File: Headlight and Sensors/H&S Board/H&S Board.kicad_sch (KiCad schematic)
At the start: 37 parts, among them J1 XT60-M, J2 XT60-M, J3 22035035, J4 Molex Micro-Fit 4 Pin, J5 XT60-M, J6 XT60-M, J7 DAQ Board, J8 Driver UI, J9 XT60-M, Q1 PSMN1R8-40YLC,115, Q2 PSMN1R8-40YLC,115, Q3 PSMN1R8-40YLC,115, U1 ASM330LHHTR, U2 UA78M05QDCYRG4Q1, U4 ADS131M04IPWR

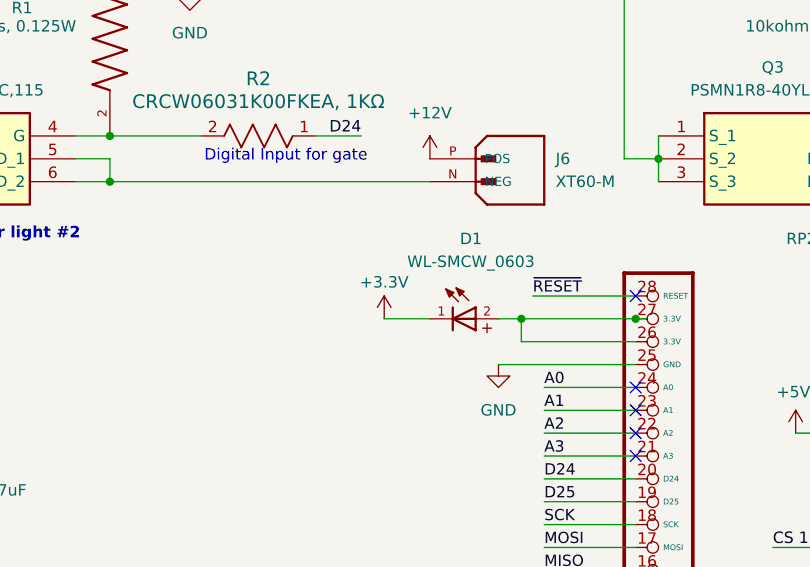
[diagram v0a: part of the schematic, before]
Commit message: fixed resistance values
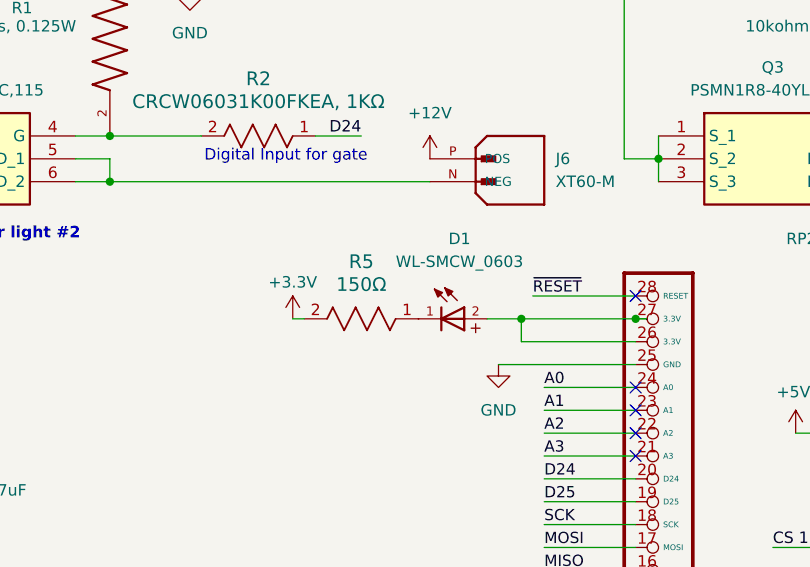
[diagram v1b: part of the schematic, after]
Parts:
- added R5: 150Ω, SMV_Passives:0805RESC2012X60N, symbol SMV_Custom:CRCW06031K00FKEA
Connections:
- net +3.3V: now also R5.2; no longer D1.1
- new net: D1.1, R5.1
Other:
- moved on the sheet: D1
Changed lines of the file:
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@@
 	(wire
 		(pts
-			(xy 171.45 54.61) (xy 166.37 54.61)
-		)
-		(stroke
-			(width 0)
-			(type default)
-		)
-	)
-	(wire
-		(pts
 			(xy 71.12 106.68) (xy 71.12 111.76)
 		)
@@
 	(wire
 		(pts
+			(xy 157.48 54.61) (xy 156.21 54.61)
+		)
+		(stroke
+			(width 0)
+			(type default)
+		)
+	)
+	(wire
+		(pts
 			(xy 205.74 133.35) (xy 208.28 133.35)
 		)
@@
 	(wire
 		(pts
-			(xy 179.07 54.61) (xy 181.61 54.61)
+			(xy 177.8 54.61) (xy 181.61 54.61)
 		)
 		(stroke
@@
 	(symbol
 		(lib_id "power:VDD")
-		(at 166.37 54.61 0)
+		(at 156.21 54.61 0)
 		(unit 1)
 		(exclude_from_sim no)
@@
 		(dnp no)
 		(property "Reference" "#PWR016"
-			(at 166.37 58.42 0)
+			(at 156.21 58.42 0)
 			(effects
 				(font
@@
 		)
 		(property "Value" "+3.3V"
-			(at 166.37 50.546 0)
+			(at 156.21 50.546 0)
 			(effects
 				(font
@@
 		)
 		(property "Footprint" ""
-			(at 166.37 54.61 0)
+			(at 156.21 54.61 0)
 			(effects
 				(font
@@
 		)
 		(property "Datasheet" ""
-			(at 166.37 54.61 0)
+			(at 156.21 54.61 0)
 			(effects
 				(font
@@
 		)
 		(property "Description" "Power symbol creates a global label with name \"VDD\""
-			(at 166.37 54.61 0)
+			(at 156.21 54.61 0)
 			(effects
 				(font
@@
 	(symbol
 		(lib_id "SMV_Custom:WL-SMCW_0603")
-		(at 173.99 54.61 0)
+		(at 172.72 54.61 0)
 		(unit 1)
 		(exclude_from_sim no)
@@
 		(fields_autoplaced yes)
 		(property "Reference" "D1"
-			(at 176.0083 45.72 0)
+			(at 174.7383 45.72 0)
 			(effects
 				(font
@@
 		)
 		(property "Value" "WL-SMCW_0603"
-			(at 176.0083 48.26 0)
+			(at 174.7383 48.26 0)
 			(effects
 				(font
@@
 		)
 		(property "Footprint" "SMV_Passives:WL-SMCW_0603(diode)"
-			(at 173.99 54.61 0)
+			(at 172.72 54.61 0)
 			(effects
 				(font
@@
 		)
 		(property "Datasheet" ""
-			(at 173.99 54.61 0)
+			(at 172.72 54.61 0)
 			(effects
 				(font
@@
 		)
 		(property "Description" ""
-			(at 173.99 54.61 0)
+			(at 172.72 54.61 0)
 			(effects
 				(font
@@
 					(unit 1)
 				)
+			)
+		)
+	)
+	(symbol
+		(lib_id "SMV_Custom:CRCW06031K00FKEA")
+		(at 157.48 54.61 0)
+		(unit 1)
+		(exclude_from_sim no)
+		(in_bom yes)
+		(on_board yes)
+		(dnp no)
+		(fields_autoplaced yes)
+		(property "Reference" "R5"
+			(at 163.83 48.26 0)
+			(effects
+				(font
+					(size 1.524 1.524)
+				)
+			)
+		)
+		(property "Value" "150Ω"
+			(at 163.83 50.8 0)
+			(effects
+				(font
+					(size 1.524 1.524)
+				)
+			)
+		)
+		(property "Footprint" "SMV_Passives:0805RESC2012X60N"
+			(at 157.48 54.61 0)
+			(effects
+				(font
+					(size 1.27 1.27)
+					(italic yes)
+				)
+				(hide yes)
+			)
+		)
+		(property "Datasheet" "CRCW06031K00FKEA"
+			(at 157.48 54.61 0)
+			(effects
+				(font
+					(size 1.27 1.27)
+					(italic yes)
+				)
+				(hide yes)
+			)
+		)
+		(property "Description" ""
+			(at 157.48 54.61 0)
+			(effects
+				(font
+					(size 1.27 1.27)
+				)
+				(hide yes)
+			)
+		)
+		(pin "1"
+		)
+		(pin "2"
+		)
+		(instances
+			(project ""
+				(path "/cdf86217-7949-4457-8f19-2e0a76b22e93"
+					(reference "R5")
+					(unit 1)
+				)

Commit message: finalized values
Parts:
- C2: value C0805C224K3RACTU -> 0.22 uF
- Q1, Q2, Q3: footprint PSMN1R840YLC115 -> MOSFET PSMN1R8-40YLC,115:PSMN1R840YLC115
- U1: footprint LGA-14L_2P5X3X0P83_STM -> Accelerometer ASM330LHHTR:LGA-14L_2P5X3X0P83_STM
- U4: footprint PW20_TEX -> ADC ADS131M04IPWR:PW20_TEX
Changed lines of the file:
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@@
 			)
 		)
-		(property "Footprint" "LGA-14L_2P5X3X0P83_STM"
+		(property "Footprint" "Accelerometer ASM330LHHTR:LGA-14L_2P5X3X0P83_STM"
 			(at 208.28 133.35 0)
 			(effects
@@
 			)
 		)
-		(property "Footprint" "PSMN1R840YLC115"
+		(property "Footprint" "MOSFET PSMN1R8-40YLC,115:PSMN1R840YLC115"
 			(at 39.37 130.48 0)
 			(effects
@@
 			)
 		)
-		(property "Value" "C0805C224K3RACTU"
+		(property "Value" "0.22 uF"
 			(at 144.78 111.7599 90)
 			(effects
@@
 			)
 		)
-		(property "Footprint" "PSMN1R840YLC115"
+		(property "Footprint" "MOSFET PSMN1R8-40YLC,115:PSMN1R840YLC115"
 			(at 218.44 129.21 0)
 			(effects
@@
 			)
 		)
-		(property "Footprint" "PW20_TEX"
+		(property "Footprint" "ADC ADS131M04IPWR:PW20_TEX"
 			(at 71.12 111.76 0)
 			(effects
@@
 			)
 		)
-		(property "Footprint" "PSMN1R840YLC115"
+		(property "Footprint" "MOSFET PSMN1R8-40YLC,115:PSMN1R840YLC115"
 			(at 128.27 129.21 0)
 			(effects

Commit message: finalizing schematic
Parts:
- removed J1, J2, J5, J6, J9: XT60-M, XT60-M:AMASS_XT60-M, symbol XT60-M Vertical:XT60-M
- added D2: LED, SMV_Passives:WL-SMCW_0603(diode), symbol SMV_Custom:WL-SMCW_0603
- added J1, J10, J2, J5, J6: 430450200, CONN_SD-43045-001_02_MOL, symbol Microfit_Molex:430450200
- added R10, R9: 40k, SMV_Passives:0805RESC2012X60N, symbol SMV_Custom:CRCW080540K0FKEA
- added R11: 150Ω, SMV_Passives:0805RESC2012X60N, symbol SMV_Custom:CRCW06031K00FKEA
- added TP5, TP6, TP7, TP8, TP9: TestPoint, TestPoint:TestPoint_Pad_D1.0mm, symbol Connector:TestPoint
- D1: value WL-SMCW_0603 -> LED
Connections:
- net A1 is gone; now on net MOSI: RP2.23 (A1)
- net A2 is gone; now on net MISO: RP2.22 (A2)
- net +12 V: now also J1.1
- net +12V: now also J10.1, J2.1, J5.1, J6.1
- net +3.3V: now also D1.2, RP2.26 (3.3V), RP2.27 (3.3V), R9.1; no longer R5.2
- net D10: no longer U4.17 (CLKIN)
- net D11: no longer U4.11 (*SYNC/*RESET)
- net D13: now also D2.2
- net D6: now also R2.1
- net GND: now also R5.2, J1.2, J10.2, R10.2, R11.2; no longer U4.10 (AIN3P)
- net MISO: now also TP7.1; no longer RP2.16 (MISO)
- net MOSI: now also TP6.1; no longer RP2.17 (MOSI)
- net SCK: now also TP9.1
- net at Q1.5 (D_1), Q1.6 (D_2): now also J5.2
- net at Q3.5 (D_1), Q3.6 (D_2): now also J6.2
- net at Q2.5 (D_1), Q2.6 (D_2): now also J2.2
- net A0 renamed GPIO_CLKIN
- net GPIO_CLKIN: now also U4.17 (CLKIN), TP5.1
- net A3: no longer names the net of RP2.21 (A3)
- net D24 renamed GPIO_RESET
- net GPIO_RESET: now also U4.11 (*SYNC/*RESET), TP8.1; no longer R2.1
- net RX: no longer names the net of RP2.15 (RX)
- net TX: no longer names the net of RP2.14 (TX)
- net ~{RESET}: no longer names the net of RP2.28 (RESET)
- new net: D2.1, R11.1
- new net: R10.1, R9.2, U4.10 (AIN3P)
- no-connect marks 15 -> 14
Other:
- moved on the sheet: D1, R5, R6, TP4

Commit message: PCB rough draft
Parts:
- removed J10: 430450200, CONN_SD-43045-001_02_MOL, symbol Microfit_Molex:430450200
- added J9: 430450200, Molex_Microfit:CONN_SD-43045-001_02_MOL, symbol Microfit_Molex:430450200
- added TP10, TP11, TP12, TP13, TP14, TP15, TP16, TP17, TP18, TP19, TP20, TP21, TP22: TestPoint, TestPoint:TestPoint_Pad_D1.0mm, symbol Connector:TestPoint
- J1, J2, J5, J6: footprint CONN_SD-43045-001_02_MOL -> Molex_Microfit:CONN_SD-43045-001_02_MOL
- J3, J7, J8: footprint CON_22035035_MOL -> SMV_Connectors:3pin_CON_22035035_MOL
- J4: footprint 0430450401 -> SMV_Connectors:4_pin0430450401
- R16, R2, R3: value CRCW06031K00FKEA, 1KΩ -> 1KΩ
- TP1: footprint TestPoint:TestPoint_Pad_D1.0mm -> TestPoint:TestPoint_Pad_D1.5mm
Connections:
- net +12 V is gone; now on net +12V: J1.1
- net +12V: now also J4.1, TP1.1, TP2.1, J9.1, TP18.1, TP19.1, TP21.1
- net +3.3V: now also U1.2 (RES), U1.3 (RES)
- net +5V: now also TP20.1; no longer J4.1
- net CS 1: now also R6.1, RP2.19 (D25), RP2.4 (D13), TP4.1, U4.12 (*CS), TP22.1; no longer RP2.8 (D9)
- net D11: now also R2.1, TP15.1
- net D12: now also D2.2; no longer U1.2 (RES), U1.3 (RES)
- net D6: now also R3.1, TP17.1; no longer R2.1
- net GND: now also U4.4 (AIN0N), U4.6 (AIN1P), J9.2; no longer U4.7 (AIN2P), U4.8 (AIN2N)
- net MISO: now also RP2.16 (MISO); no longer TP2.1
- net MOSI: now also RP2.17 (MOSI)
- net Press_ADC_P: now also U4.3 (AIN0P); no longer U4.6 (AIN1P)
- net Press_P: now also TP12.1
- net SCK: no longer TP1.1
- net Torque_ADC_N: now also U4.8 (AIN2N); no longer U4.4 (AIN0N)
- net Torque_ADC_P: now also U4.7 (AIN2P); no longer U4.3 (AIN0P)
- net Torque_N: now also TP14.1
- net Torque_P: now also TP13.1
- net CAN_N: now reaches J7.1, J8.1, RP2.29 (CAN_L)
- net CAN_N: now also TP11.1
- net CAN_P: now reaches J7.3, J8.3, RP2.31 (CAN_H)
- net CAN_P: now also TP10.1
- net Test_Divider: now reaches R10.1, R9.2, U4.10 (AIN3P)
- removed net CS 0: R6.1, RP2.10 (D5), TP4.1, U4.12 (*CS)
- removed net D13: D2.2, RP2.4 (D13)
- removed net D25: R3.1, RP2.19 (D25)
- net D4: no longer names the net of RP2.13 (D4)
- net D4: no longer R16.1
- new net D5: R16.1, RP2.10 (D5), TP16.1
- new net D9: RP2.8 (D9)
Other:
- moved on the sheet: C6, D2, J7, J8, R10, R11, R2, R8, R9, TP3

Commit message: basically done
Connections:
- net CS 1: no longer R8.1, RP2.4 (D13), TP22.1, U1.12 (CS)
- net MISO: no longer RP2.16 (MISO)
- net MOSI: no longer RP2.17 (MOSI)
- new net CS 0: R8.1, RP2.4 (D13), TP22.1, U1.12 (CS)
- no-connect marks 14 -> 16
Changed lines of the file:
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@@
+	)
+	(no_connect
+		(at 194.31 80.01)
 	)
 	(no_connect
@@
 	)
 	(no_connect
+		(at 194.31 82.55)
+	)
+	(no_connect
 		(at 215.9 90.17)
 	)
@@
 	(wire
 		(pts
-			(xy 187.96 80.01) (xy 194.31 80.01)
-		)
-		(stroke
-			(width 0)
-			(type default)
-		)
-	)
-	(wire
-		(pts
 			(xy 102.87 36.83) (xy 102.87 13.97)
 		)
@@
 		(pts
 			(xy 185.42 57.15) (xy 194.31 57.15)
-		)
-		(stroke
-			(width 0)
-			(type default)
-		)
-	)
-	(wire
-		(pts
-			(xy 187.96 82.55) (xy 194.31 82.55)
 		)
 		(stroke
@@
 		)
 	)
-	(label "MISO"
-		(at 187.96 82.55 0)
-		(fields_autoplaced yes)
-		(effects
-			(font
-				(size 1.27 1.27)
-			)
-			(justify left bottom)
-		)
-	)
 	(label "MOSI"
 		(at 187.96 64.77 0)
@@
 		)
 	)
-	(label "CS 1"
+	(label "CS 0"
 		(at 259.08 138.43 180)
 		(fields_autoplaced yes)
@@
 		)
 	)
-	(label "MOSI"
-		(at 187.96 80.01 0)
-		(fields_autoplaced yes)
-		(effects
-			(font
-				(size 1.27 1.27)
-			)
-			(justify left bottom)
-		)
-	)
 	(label "Press_P"
 		(at 13.97 127 0)
@@
 		)
 	)
-	(label "CS 1"
+	(label "CS 0"
 		(at 215.9 69.85 0)
 		(fields_autoplaced yes)

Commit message: Finished!
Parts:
- removed TP18, TP2, TP21: TestPoint, TestPoint:TestPoint_Pad_D1.0mm, symbol Connector:TestPoint
- added H1, H2, H3, H4: MountingHole, MountingHole:MountingHole_3.2mm_M3, symbol Mechanical:MountingHole
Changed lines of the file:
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@@
 	)
 	(junction
-		(at 262.89 36.83)
-		(diameter 0)
-		(color 0 0 0 0)
-	)
-	(junction
 		(at 257.81 148.59)
 		(diameter 0)
@@
 	)
 	(junction
-		(at 76.2 181.61)
-		(diameter 0)
-		(color 0 0 0 0)
-	)
-	(junction
 		(at 66.04 114.3)
 		(diameter 0)
@@
 	)
 	(junction
-		(at 171.45 36.83)
-		(diameter 0)
-		(color 0 0 0 0)
-	)
-	(junction
 		(at 204.47 148.59)
 		(diameter 0)
@@
 	(wire
 		(pts
-			(xy 76.2 181.61) (xy 83.82 181.61)
+			(xy 62.23 181.61) (xy 83.82 181.61)
 		)
 		(stroke
@@
 	(wire
 		(pts
-			(xy 62.23 181.61) (xy 76.2 181.61)
-		)
-		(stroke
-			(width 0)
-			(type default)
-		)
-	)
-	(wire
-		(pts
 			(xy 196.85 111.76) (xy 199.39 111.76)
 		)
@@
 	)
 	(symbol
-		(lib_id "Connector:TestPoint")
-		(at 262.89 36.83 0)
-		(unit 1)
-		(exclude_from_sim no)
-		(in_bom yes)
-		(on_board yes)
-		(dnp no)
-		(property "Reference" "TP18"
-			(at 272.288 30.988 0)
-			(effects
-				(font
-					(size 1.27 1.27)
-				)
-				(justify left)
-			)
-		)
-		(property "Value" "TestPoint"
-			(at 262.89 30.988 0)
-			(effects
-				(font
-					(size 1.27 1.27)
-				)
-				(justify left)
-			)
-		)
-		(property "Footprint" "TestPoint:TestPoint_Pad_D1.0mm"
-			(at 267.97 36.83 0)
-			(effects
-				(font
-					(size 1.27 1.27)
-				)
-				(hide yes)
-			)
-		)
-		(property "Datasheet" "~"
-			(at 267.97 36.83 0)
-			(effects
-				(font
-					(size 1.27 1.27)
-				)
-				(hide yes)
-			)
-		)
-		(property "Description" "test point"
-			(at 262.89 36.83 0)
-			(effects
-				(font
-					(size 1.27 1.27)
-				)
-				(hide yes)
-			)
-		)
-		(pin "1"
-		)
-		(instances
-			(project "H&S Board"
-				(path "/cdf86217-7949-4457-8f19-2e0a76b22e93"
-					(reference "TP18")
-					(unit 1)
-				)
-			)
-		)
-	)
-	(symbol
-		(lib_id "Connector:TestPoint")
-		(at 171.45 36.83 0)
+		(lib_id "Mechanical:MountingHole")
+		(at 139.7 71.12 0)
 		(unit 1)
-		(exclude_from_sim no)
-		(in_bom yes)
+		(exclude_from_sim yes)
+		(in_bom no)
 		(on_board yes)
 		(dnp no)
-		(property "Reference" "TP2"
-			(at 180.848 30.988 0)
+		(fields_autoplaced yes)
+		(property "Reference" "H4"
+			(at 142.24 69.8499 0)
 			(effects
 				(font
@@
 			)
 		)
-		(property "Value" "TestPoint"
-			(at 171.45 30.988 0)
+		(property "Value" "MountingHole"
+			(at 142.24 72.3899 0)
 			(effects
 				(font
@@
 			)
 		)
-		(property "Footprint" "TestPoint:TestPoint_Pad_D1.0mm"
-			(at 176.53 36.83 0)
+		(property "Footprint" "MountingHole:MountingHole_3.2mm_M3"
+			(at 139.7 71.12 0)
 			(effects
 				(font
@@
 		)
 		(property "Datasheet" "~"
-			(at 176.53 36.83 0)
+			(at 139.7 71.12 0)
 			(effects
 				(font
@@
 			)
 		)
-		(property "Description" "test point"
-			(at 171.45 36.83 0)
+		(property "Description" "Mounting Hole without connection"
+			(at 139.7 71.12 0)
 			(effects
 				(font
@@
 			)
 		)
-		(pin "1"
-		)
 		(instances
 			(project "H&S Board"
 				(path "/cdf86217-7949-4457-8f19-2e0a76b22e93"
-					(reference "TP2")
+					(reference "H4")
 					(unit 1)
 				)
@@
 	)
 	(symbol
+		(lib_id "Mechanical:MountingHole")
+		(at 139.7 58.42 0)
+		(unit 1)
+		(exclude_from_sim yes)
+		(in_bom no)
+		(on_board yes)
+		(dnp no)
+		(fields_autoplaced yes)
+		(property "Reference" "H2"
+			(at 142.24 57.1499 0)
+			(effects
+				(font
+					(size 1.27 1.27)
+				)
+				(justify left)
+			)
+		)
+		(property "Value" "MountingHole"
+			(at 142.24 59.6899 0)
+			(effects
+				(font
+					(size 1.27 1.27)
+				)
+				(justify left)
+			)
+		)
+		(property "Footprint" "MountingHole:MountingHole_3.2mm_M3"
+			(at 139.7 58.42 0)
+			(effects
+				(font
+					(size 1.27 1.27)
+				)
+				(hide yes)
+			)
+		)
+		(property "Datasheet" "~"
+			(at 139.7 58.42 0)
+			(effects
+				(font
+					(size 1.27 1.27)
+				)
+				(hide yes)
+			)
+		)
+		(property "Description" "Mounting Hole without connection"
+			(at 139.7 58.42 0)
+			(effects
+				(font
+					(size 1.27 1.27)
+				)
+				(hide yes)
+			)
+		)
+		(instances
+			(project "H&S Board"
+				(path "/cdf86217-7949-4457-8f19-2e0a76b22e93"
+					(reference "H2")
+					(unit 1)
+				)
+			)
+		)
+	)
+	(symbol
 		(lib_id "Microfit_Molex:430450200")
 		(at 81.28 38.1 0)
@@
 	)
 	(symbol
+		(lib_id "Mechanical:MountingHole")
+		(at 139.7 52.07 0)
+		(unit 1)
+		(exclude_from_sim yes)
+		(in_bom no)
+		(on_board yes)
+		(dnp no)
+		(fields_autoplaced yes)
+		(property "Reference" "H1"
+			(at 142.24 50.7999 0)
+			(effects
+				(font
+					(size 1.27 1.27)
+				)
+				(justify left)
+			)
+		)
+		(property "Value" "MountingHole"
+			(at 142.24 53.3399 0)
+			(effects
+				(font
+					(size 1.27 1.27)
+				)
+				(justify left)
+			)
+		)
+		(property "Footprint" "MountingHole:MountingHole_3.2mm_M3"
+			(at 139.7 52.07 0)
+			(effects
+				(font
+					(size 1.27 1.27)
+				)
+				(hide yes)
+			)
+		)
+		(property "Datasheet" "~"
+			(at 139.7 52.07 0)
+			(effects
+				(font
+					(size 1.27 1.27)
+				)
+				(hide yes)
+			)
+		)
+		(property "Description" "Mounting Hole without connection"
+			(at 139.7 52.07 0)
+			(effects
+				(font
+					(size 1.27 1.27)
+				)
+				(hide yes)
+			)
+		)
+		(instances
+			(project ""
+				(path "/cdf86217-7949-4457-8f19-2e0a76b22e93"
+					(reference "H1")
+					(unit 1)
+				)
+			)
+		)
+	)
+	(symbol
 		(lib_id "Microfit_Molex:430450200")
 		(at 257.81 86.36 0)
@@
 	)
 	(symbol
+		(lib_id "Mechanical:MountingHole")
+		(at 139.7 64.77 0)
+		(unit 1)
+		(exclude_from_sim yes)
+		(in_bom no)
+		(on_board yes)
+		(dnp no)
+		(fields_autoplaced yes)
+		(property "Reference" "H3"
+			(at 142.24 63.4999 0)
+			(effects
+				(font
+					(size 1.27 1.27)
+				)
+				(justify left)
+			)
+		)
+		(property "Value" "MountingHole"
+			(at 142.24 66.0399 0)
+			(effects
+				(font
+					(size 1.27 1.27)
+				)
+				(justify left)
+			)
+		)
+		(property "Footprint" "MountingHole:MountingHole_3.2mm_M3"
+			(at 139.7 64.77 0)
+			(effects
+				(font
+					(size 1.27 1.27)
+				)
+				(hide yes)
+			)
+		)
+		(property "Datasheet" "~"
+			(at 139.7 64.77 0)
+			(effects
+				(font
+					(size 1.27 1.27)
+				)
+				(hide yes)
+			)
+		)
+		(property "Description" "Mounting Hole without connection"
+			(at 139.7 64.77 0)
+			(effects
+				(font
+					(size 1.27 1.27)
+				)
+				(hide yes)
+			)
+		)
+		(instances
+			(project "H&S Board"
+				(path "/cdf86217-7949-4457-8f19-2e0a76b22e93"
+					(reference "H3")
+					(unit 1)
+				)
+			)
+		)
+	)
+	(symbol
 		(lib_id "power:GND")
 		(at 158.75 54.61 0)
@@
 					(unit 1)
 				)
-			)
-		)
-	)
-	(symbol
-		(lib_id "Connector:TestPoint")
-		(at 76.2 181.61 0)
-		(unit 1)
-		(exclude_from_sim no)
-		(in_bom yes)
-		(on_board yes)
-		(dnp no)
-		(property "Reference" "TP21"
-			(at 73.914 174.244 0)
-			(effects
-				(font
-					(size 1.27 1.27)
-				)
-				(justify left)
-			)
-		)
-		(property "Value" "TestPoint"
-			(at 71.882 176.276 0)
-			(effects
-				(font
-					(size 1.27 1.27)
-				)
-				(justify left)
-			)
-		)
-		(property "Footprint" "TestPoint:TestPoint_Pad_D1.0mm"
-			(at 81.28 181.61 0)
-			(effects
-				(font
-					(size 1.27 1.27)
-				)
-				(hide yes)
-			)
-		)
-		(property "Datasheet" "~"
-			(at 81.28 181.61 0)
-			(effects
-				(font
-					(size 1.27 1.27)
-				)
-				(hide yes)
-			)
-		)
-		(property "Description" "test point"
-			(at 76.2 181.61 0)
-			(effects
-				(font
-					(size 1.27 1.27)
-				)
-				(hide yes)
-			)
-		)
-		(pin "1"
-		)
-		(instances
-			(project "H&S Board"
-				(path "/cdf86217-7949-4457-8f19-2e0a76b22e93"
-					(reference "TP21")
-					(unit 1)
-				)
